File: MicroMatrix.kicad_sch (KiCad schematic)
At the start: 66 parts, among them J1 Conn_01x03, J2 Conn_01x03

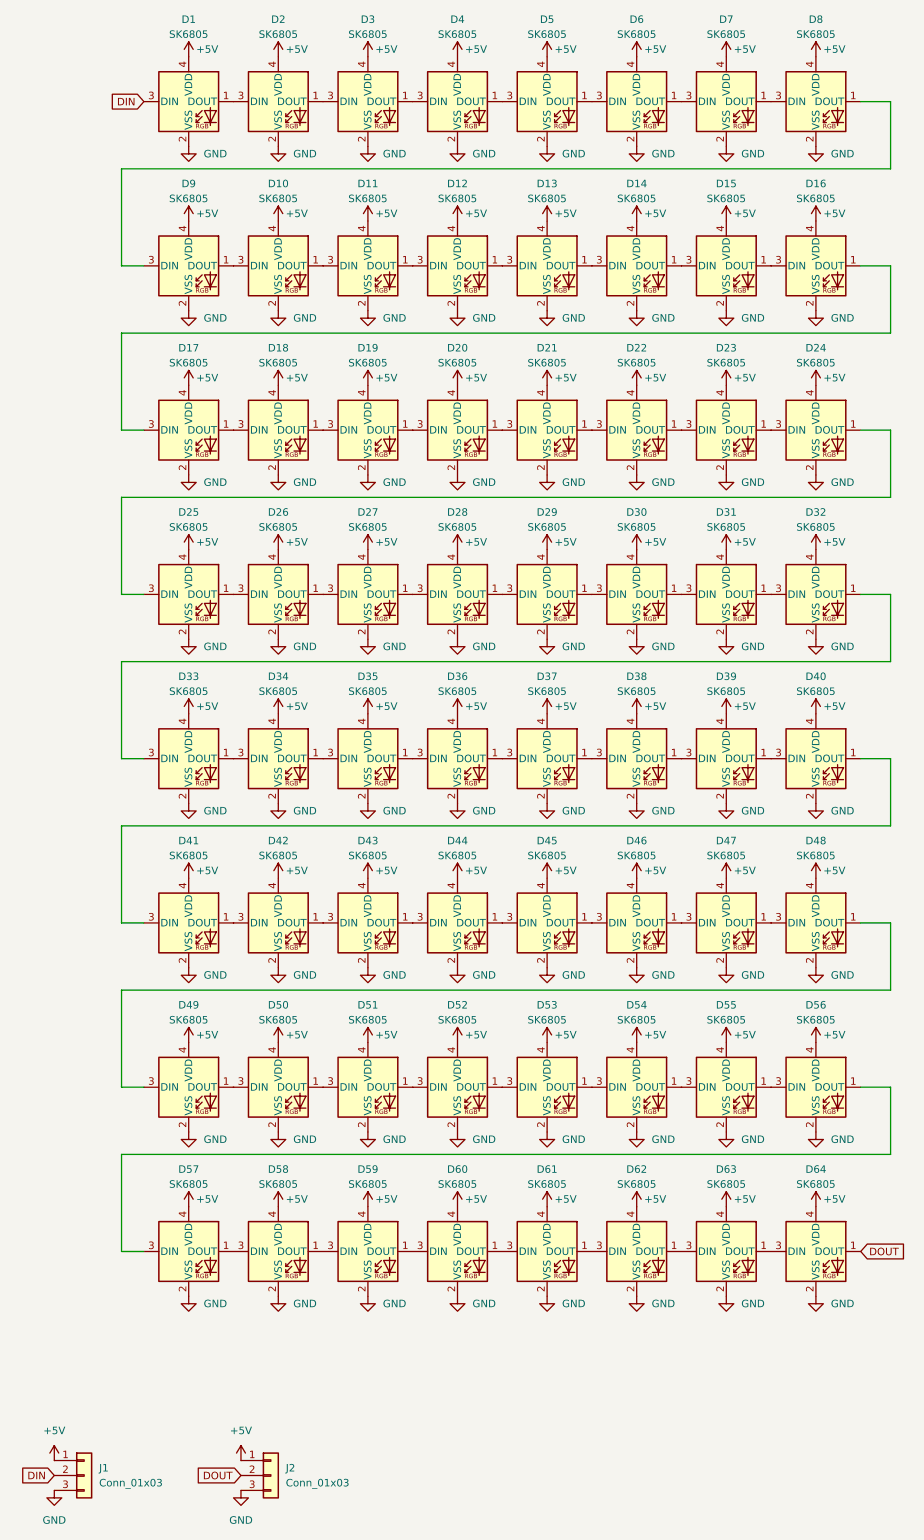
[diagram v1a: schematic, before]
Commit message: Updated PCB to REV1.3 Replaced SK6805 footprint/symbol with a own version
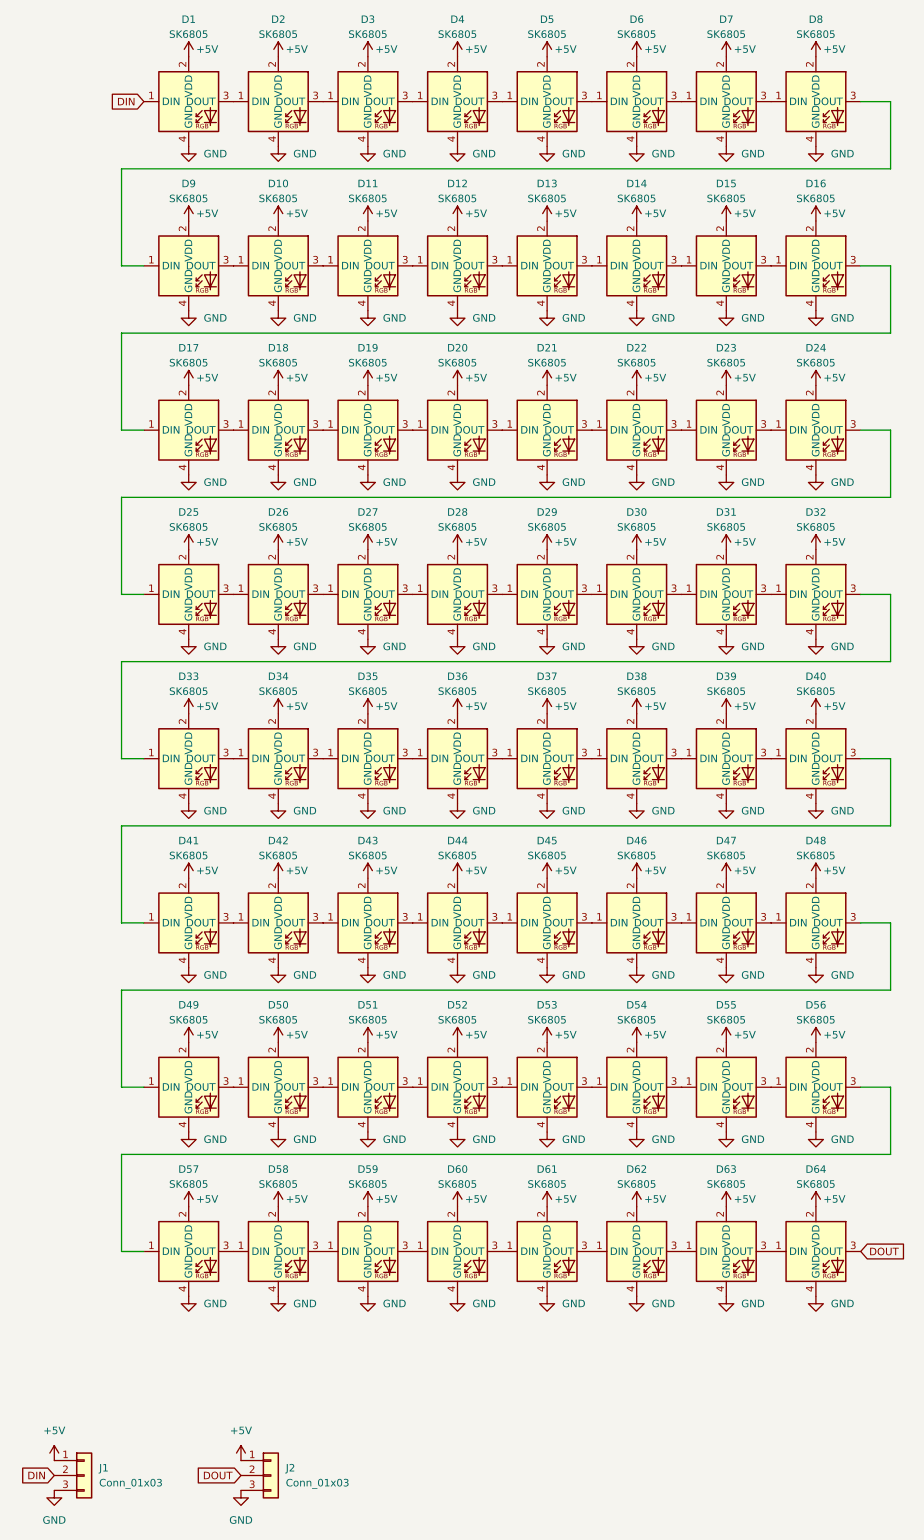
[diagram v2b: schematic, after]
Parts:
- D1, D10, D11, D12, D13, D14, D15, D16, D17, D18, D19, D2, D20, D21, D22, D23, D24, D25, D26, D27, D28, D29, D3, D30, D31, D32, D33, D34, D35, D36, D37, D38, D39, D4, D40, D41, D42, D43, D44, D45, D46, D47, D48, D49, D5, D50, D51, D52, D53, D54, D55, D56, D57, D58, D59, D6, D60, D61, D62, D63, D64, D7, D8, D9: footprint LED_SMD:LED_SK6812_EC15_1.5x1.5mm -> SK6805-EC15:SK6805-EC15; symbol LED:SK6805 -> SK6805-EC15:SK6805-EC15
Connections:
- net +5V: now also D1.2 (VDD), D10.2 (VDD), D11.2 (VDD), D12.2 (VDD), D13.2 (VDD), D14.2 (VDD), D15.2 (VDD), D16.2 (VDD), D17.2 (VDD), D18.2 (VDD), D19.2 (VDD), D2.2 (VDD), D20.2 (VDD), D21.2 (VDD), D22.2 (VDD), D23.2 (VDD), D24.2 (VDD), D25.2 (VDD), D26.2 (VDD), D27.2 (VDD), D28.2 (VDD), D29.2 (VDD), D3.2 (VDD), D30.2 (VDD), D31.2 (VDD), D32.2 (VDD), D33.2 (VDD), D34.2 (VDD), D35.2 (VDD), D36.2 (VDD), D37.2 (VDD), D38.2 (VDD), D39.2 (VDD), D4.2 (VDD), D40.2 (VDD), D41.2 (VDD), D42.2 (VDD), D43.2 (VDD), D44.2 (VDD), D45.2 (VDD), D46.2 (VDD), D47.2 (VDD), D48.2 (VDD), D49.2 (VDD), D5.2 (VDD), D50.2 (VDD), D51.2 (VDD), D52.2 (VDD), D53.2 (VDD), D54.2 (VDD), D55.2 (VDD), D56.2 (VDD), D57.2 (VDD), D58.2 (VDD), D59.2 (VDD), D6.2 (VDD), D60.2 (VDD), D61.2 (VDD), D62.2 (VDD), D63.2 (VDD), D64.2 (VDD), D7.2 (VDD), D8.2 (VDD), D9.2 (VDD); no longer D1.4 (VDD), D10.4 (VDD), D11.4 (VDD), D12.4 (VDD), D13.4 (VDD), D14.4 (VDD), D15.4 (VDD), D16.4 (VDD), D17.4 (VDD), D18.4 (VDD), D19.4 (VDD), D2.4 (VDD), D20.4 (VDD), D21.4 (VDD), D22.4 (VDD), D23.4 (VDD), D24.4 (VDD), D25.4 (VDD), D26.4 (VDD), D27.4 (VDD), D28.4 (VDD), D29.4 (VDD), D3.4 (VDD), D30.4 (VDD), D31.4 (VDD), D32.4 (VDD), D33.4 (VDD), D34.4 (VDD), D35.4 (VDD), D36.4 (VDD), D37.4 (VDD), D38.4 (VDD), D39.4 (VDD), D4.4 (VDD), D40.4 (VDD), D41.4 (VDD), D42.4 (VDD), D43.4 (VDD), D44.4 (VDD), D45.4 (VDD), D46.4 (VDD), D47.4 (VDD), D48.4 (VDD), D49.4 (VDD), D5.4 (VDD), D50.4 (VDD), D51.4 (VDD), D52.4 (VDD), D53.4 (VDD), D54.4 (VDD), D55.4 (VDD), D56.4 (VDD), D57.4 (VDD), D58.4 (VDD), D59.4 (VDD), D6.4 (VDD), D60.4 (VDD), D61.4 (VDD), D62.4 (VDD), D63.4 (VDD), D64.4 (VDD), D7.4 (VDD), D8.4 (VDD), D9.4 (VDD)
- net DIN: now also D1.1 (DIN); no longer D1.3 (DIN)
- net DOUT: now also D64.3 (DOUT); no longer D64.1 (DOUT)
- net GND: now also D1.4 (GND), D10.4 (GND), D11.4 (GND), D12.4 (GND), D13.4 (GND), D14.4 (GND), D15.4 (GND), D16.4 (GND), D17.4 (GND), D18.4 (GND), D19.4 (GND), D2.4 (GND), D20.4 (GND), D21.4 (GND), D22.4 (GND), D23.4 (GND), D24.4 (GND), D25.4 (GND), D26.4 (GND), D27.4 (GND), D28.4 (GND), D29.4 (GND), D3.4 (GND), D30.4 (GND), D31.4 (GND), D32.4 (GND), D33.4 (GND), D34.4 (GND), D35.4 (GND), D36.4 (GND), D37.4 (GND), D38.4 (GND), D39.4 (GND), D4.4 (GND), D40.4 (GND), D41.4 (GND), D42.4 (GND), D43.4 (GND), D44.4 (GND), D45.4 (GND), D46.4 (GND), D47.4 (GND), D48.4 (GND), D49.4 (GND), D5.4 (GND), D50.4 (GND), D51.4 (GND), D52.4 (GND), D53.4 (GND), D54.4 (GND), D55.4 (GND), D56.4 (GND), D57.4 (GND), D58.4 (GND), D59.4 (GND), D6.4 (GND), D60.4 (GND), D61.4 (GND), D62.4 (GND), D63.4 (GND), D64.4 (GND), D7.4 (GND), D8.4 (GND), D9.4 (GND); no longer D1.2 (VSS), D10.2 (VSS), D11.2 (VSS), D12.2 (VSS), D13.2 (VSS), D14.2 (VSS), D15.2 (VSS), D16.2 (VSS), D17.2 (VSS), D18.2 (VSS), D19.2 (VSS), D2.2 (VSS), D20.2 (VSS), D21.2 (VSS), D22.2 (VSS), D23.2 (VSS), D24.2 (VSS), D25.2 (VSS), D26.2 (VSS), D27.2 (VSS), D28.2 (VSS), D29.2 (VSS), D3.2 (VSS), D30.2 (VSS), D31.2 (VSS), D32.2 (VSS), D33.2 (VSS), D34.2 (VSS), D35.2 (VSS), D36.2 (VSS), D37.2 (VSS), D38.2 (VSS), D39.2 (VSS), D4.2 (VSS), D40.2 (VSS), D41.2 (VSS), D42.2 (VSS), D43.2 (VSS), D44.2 (VSS), D45.2 (VSS), D46.2 (VSS), D47.2 (VSS), D48.2 (VSS), D49.2 (VSS), D5.2 (VSS), D50.2 (VSS), D51.2 (VSS), D52.2 (VSS), D53.2 (VSS), D54.2 (VSS), D55.2 (VSS), D56.2 (VSS), D57.2 (VSS), D58.2 (VSS), D59.2 (VSS), D6.2 (VSS), D60.2 (VSS), D61.2 (VSS), D62.2 (VSS), D63.2 (VSS), D64.2 (VSS), D7.2 (VSS), D8.2 (VSS), D9.2 (VSS)
- net at D35.1 (DIN): now also D34.3 (DOUT); no longer D36.3 (DIN)
- net at D35.3 (DOUT): now also D36.1 (DIN); no longer D34.1 (DOUT)
- net at D59.1 (DIN): now also D58.3 (DOUT); no longer D60.3 (DIN)
- net at D59.3 (DOUT): now also D60.1 (DIN); no longer D58.1 (DOUT)
- net at D38.1 (DIN): now also D37.3 (DOUT); no longer D39.3 (DIN)
- net at D38.3 (DOUT): now also D39.1 (DIN); no longer D37.1 (DOUT)
- net at D40.3 (DOUT): now also D41.1 (DIN); no longer D39.1 (DOUT)
- net at D7.1 (DIN): now also D6.3 (DOUT); no longer D8.3 (DIN)
- net at D7.3 (DOUT): now also D8.1 (DIN); no longer D6.1 (DOUT)
- net at D2.3 (DOUT): now also D3.1 (DIN); no longer D1.1 (DOUT)
- net at D33.1 (DIN): now also D32.3 (DOUT); no longer D34.3 (DIN)
- net at D44.1 (DIN): now also D43.3 (DOUT); no longer D45.3 (DIN)
- net at D44.3 (DOUT): now also D45.1 (DIN); no longer D43.1 (DOUT)
- net at D47.1 (DIN): now also D46.3 (DOUT); no longer D48.3 (DIN)
- net at D47.3 (DOUT): now also D48.1 (DIN); no longer D46.1 (DOUT)
- net at D27.1 (DIN): now also D26.3 (DOUT); no longer D28.3 (DIN)
- net at D27.3 (DOUT): now also D28.1 (DIN); no longer D26.1 (DOUT)
- net at D17.1 (DIN): now also D16.3 (DOUT); no longer D18.3 (DIN)
- net at D17.3 (DOUT): now also D18.1 (DIN); no longer D16.1 (DOUT)
- net at D12.1 (DIN): now also D11.3 (DOUT); no longer D13.3 (DIN)
- net at D12.3 (DOUT): now also D13.1 (DIN); no longer D11.1 (DOUT)
- net at D50.1 (DIN): now also D49.3 (DOUT); no longer D51.3 (DIN)
- net at D50.3 (DOUT): now also D51.1 (DIN); no longer D49.1 (DOUT)
- net at D5.1 (DIN): now also D4.3 (DOUT); no longer D6.3 (DIN)
- net at D52.1 (DIN): now also D51.3 (DOUT); no longer D53.3 (DIN)
- net at D52.3 (DOUT): now also D53.1 (DIN); no longer D51.1 (DOUT)
- net at D55.1 (DIN): now also D54.3 (DOUT); no longer D56.3 (DIN)
- net at D55.3 (DOUT): now also D56.1 (DIN); no longer D54.1 (DOUT)
- net at D63.1 (DIN): now also D62.3 (DOUT); no longer D64.3 (DIN)
- net at D42.1 (DIN): now also D41.3 (DOUT); no longer D43.3 (DIN)
- net at D9.3 (DOUT): now also D10.1 (DIN); no longer D8.1 (DOUT)
- net at D42.3 (DOUT): now also D43.1 (DIN); no longer D41.1 (DOUT)
- net at D40.1 (DIN): now also D39.3 (DOUT); no longer D41.3 (DIN)
- net at D33.3 (DOUT): now also D34.1 (DIN); no longer D32.1 (DOUT)
- net at D61.1 (DIN): now also D60.3 (DOUT); no longer D62.3 (DIN)
- net at D61.3 (DOUT): now also D62.1 (DIN); no longer D60.1 (DOUT)
- net at D30.1 (DIN): now also D29.3 (DOUT); no longer D31.3 (DIN)
- net at D30.3 (DOUT): now also D31.1 (DIN); no longer D29.1 (DOUT)
- net at D23.1 (DIN): now also D22.3 (DOUT); no longer D24.3 (DIN)
- net at D23.3 (DOUT): now also D24.1 (DIN); no longer D22.1 (DOUT)
- net at D5.3 (DOUT): now also D6.1 (DIN); no longer D4.1 (DOUT)
- net at D63.3 (DOUT): now also D64.1 (DIN); no longer D62.1 (DOUT)
- net at D57.1 (DIN): now also D56.3 (DOUT); no longer D58.3 (DIN)
- net at D21.1 (DIN): now also D20.3 (DOUT); no longer D22.3 (DIN)
- net at D21.3 (DOUT): now also D22.1 (DIN); no longer D20.1 (DOUT)
- net at D14.3 (DOUT): now also D15.1 (DIN); no longer D13.1 (DOUT)
- net at D57.3 (DOUT): now also D58.1 (DIN); no longer D56.1 (DOUT)
- net at D2.1 (DIN): now also D1.3 (DOUT); no longer D3.3 (DIN)
- net at D19.3 (DOUT): now also D20.1 (DIN); no longer D18.1 (DOUT)
- net at D14.1 (DIN): now also D13.3 (DOUT); no longer D15.3 (DIN)
- net at D25.3 (DOUT): now also D26.1 (DIN); no longer D24.1 (DOUT)
- net at D9.1 (DIN): now also D8.3 (DOUT); no longer D10.3 (DIN)
- net at D25.1 (DIN): now also D24.3 (DOUT); no longer D26.3 (DIN)
- net at D19.1 (DIN): now also D18.3 (DOUT); no longer D20.3 (DIN)
- new net: D36.3 (DOUT), D37.1 (DIN)
- new net: D53.3 (DOUT), D54.1 (DIN)
- new net: D28.3 (DOUT), D29.1 (DIN)
- new net: D45.3 (DOUT), D46.1 (DIN)
- new net: D15.3 (DOUT), D16.1 (DIN)
- new net: D3.3 (DOUT), D4.1 (DIN)
- new net: D48.3 (DOUT), D49.1 (DIN)
- new net: D31.3 (DOUT), D32.1 (DIN)
- new net: D10.3 (DOUT), D11.1 (DIN)
